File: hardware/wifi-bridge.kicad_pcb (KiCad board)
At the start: 4 copper layers, 50 x 35 mm, 78 parts, among them J201 USB-MINI-B-SMD, P101 CONN_1, P102 CONN_1, P103 CONN_1, P104 CON-SENSOR, Q101 MOS_P, SW101 ERASE, SW102 RESET, U101 AT91SAM3SXB, U102 ESP8266_WROOM02, U103 M24C64, U104 DRILL, U105 DRILL, U106 DRILL, U107 DRILL, U201 82400152, U202 AAT3681A, U203 PAM2301, U204 FAN4860, X101 16MHz

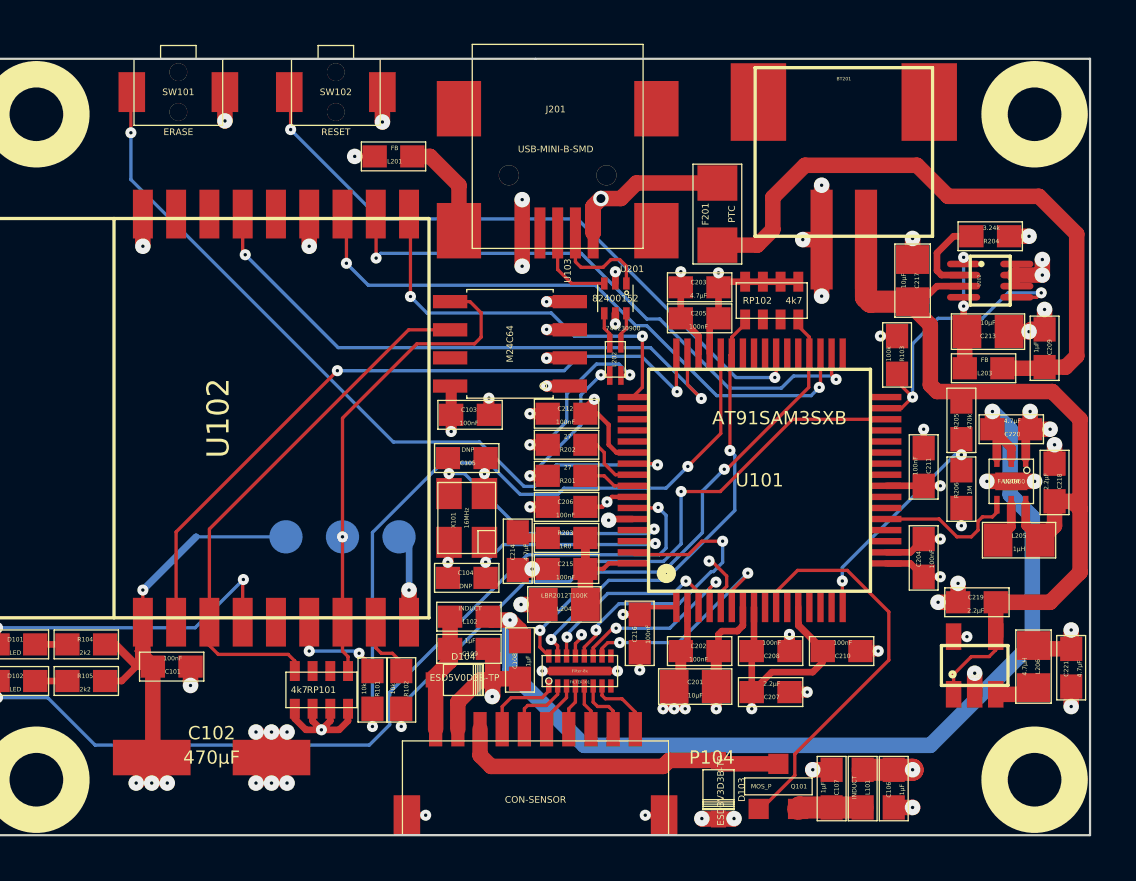
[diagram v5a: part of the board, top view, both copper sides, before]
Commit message: add planes, add logos etc.
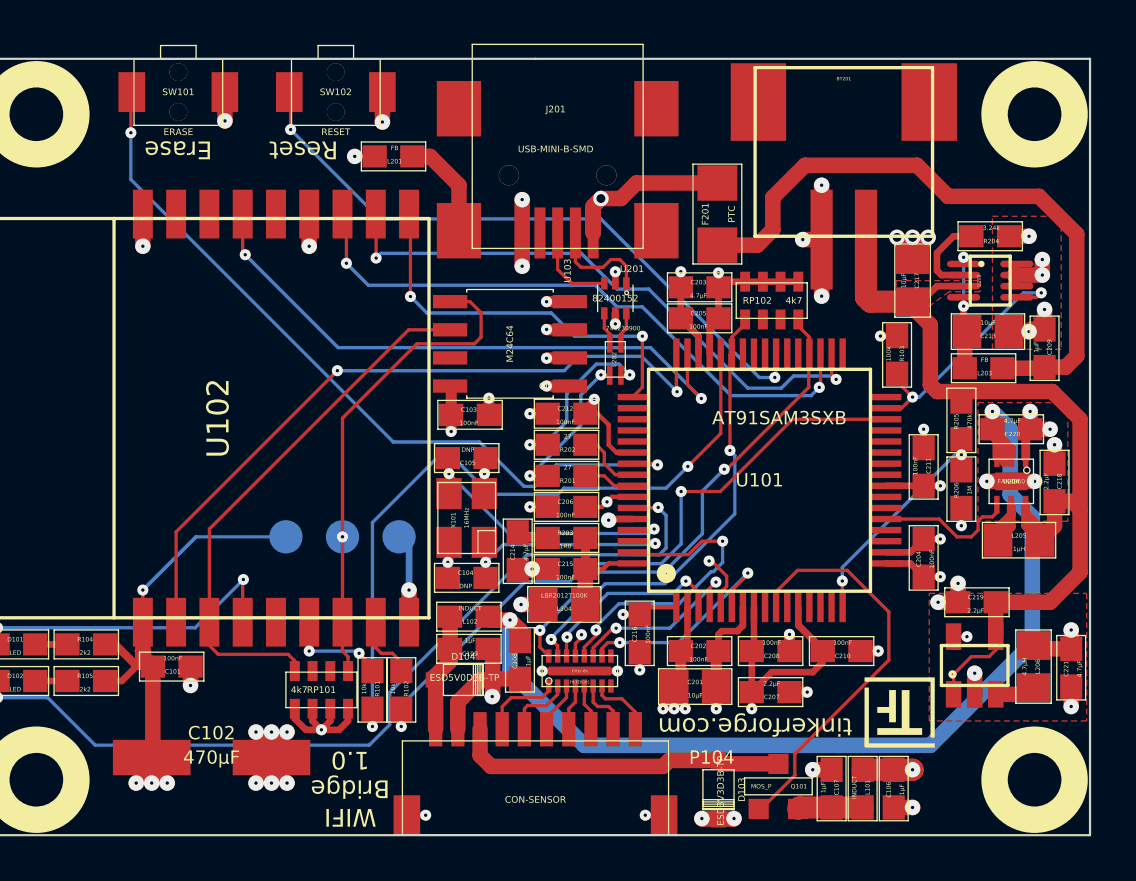
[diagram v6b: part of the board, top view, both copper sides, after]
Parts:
- added G***: Logo_31x31, kicad-libraries:Logo_31x31, F.Cu at (165.8, 46.2)
- added VAL: WEEE_7mm_back, kicad-libraries:WEEE_7mm_back, B.Cu at (147.8, 36.9)
- added VAL: CE_5mm, kicad-libraries:CE_5mm, B.Cu at (147.8, 26.8)
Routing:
- net Net-(C207-Pad1): track 58.6 -> 61.1 mm
- net GND: track 280.6 -> 282.9 mm, vias 64 -> 66
- net VCC: track 41.7 -> 43.5 mm
- net +5V: track 46.4 -> 48.1 mm
- net CHST: track 13.1 -> 11.7 mm
- net Net-(L205-Pad2): track 1.85 -> 3.25 mm
- added copper zone on VCC, net 3V3
- added copper zone on F.Cu, net GND
- added copper zone on GND, net GND
- added copper zone on F.Cu, net VCC
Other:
- board text added: "3V3"
- board text added: "DBG"
- board text added: "Erase"
- board text added: "GND"
- board text added: "Reset"
- board text added: "WIFI Bridge 1.0"
- board text added: "tinkerforge.com"

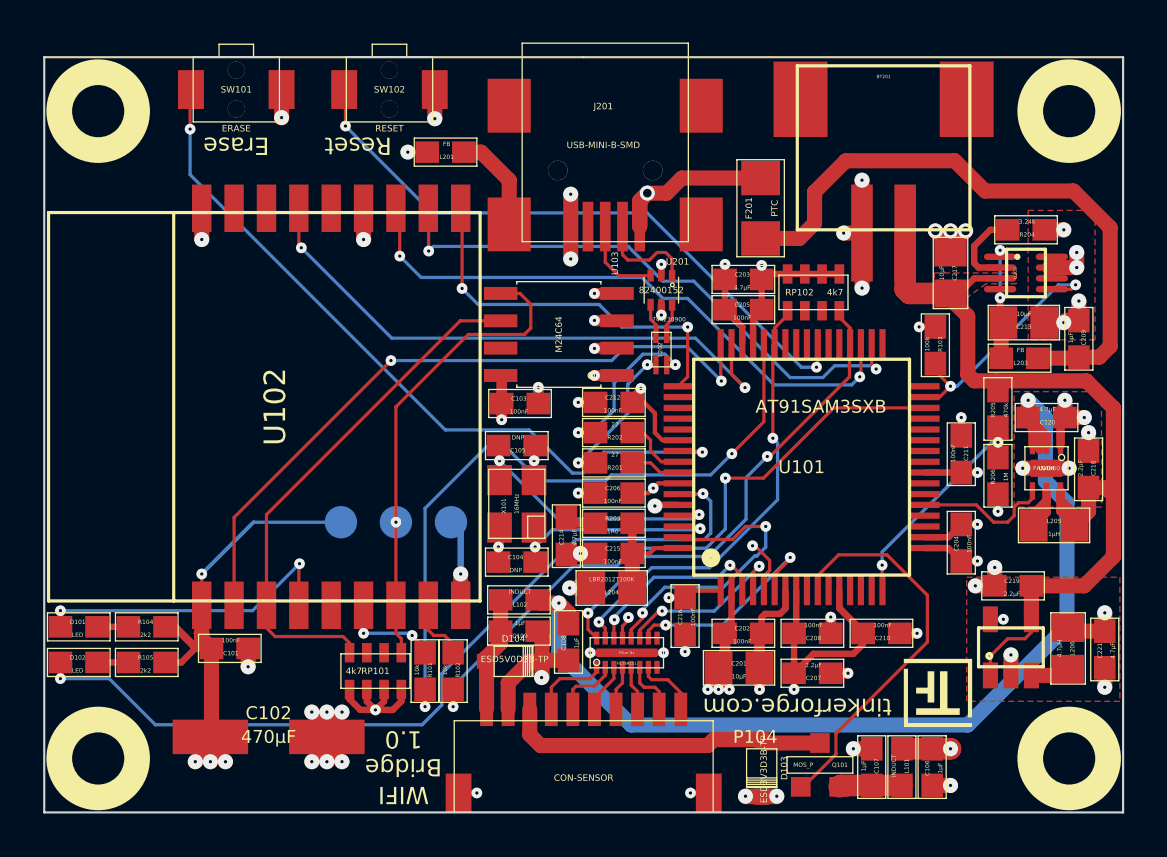
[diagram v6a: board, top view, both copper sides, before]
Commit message: round corners
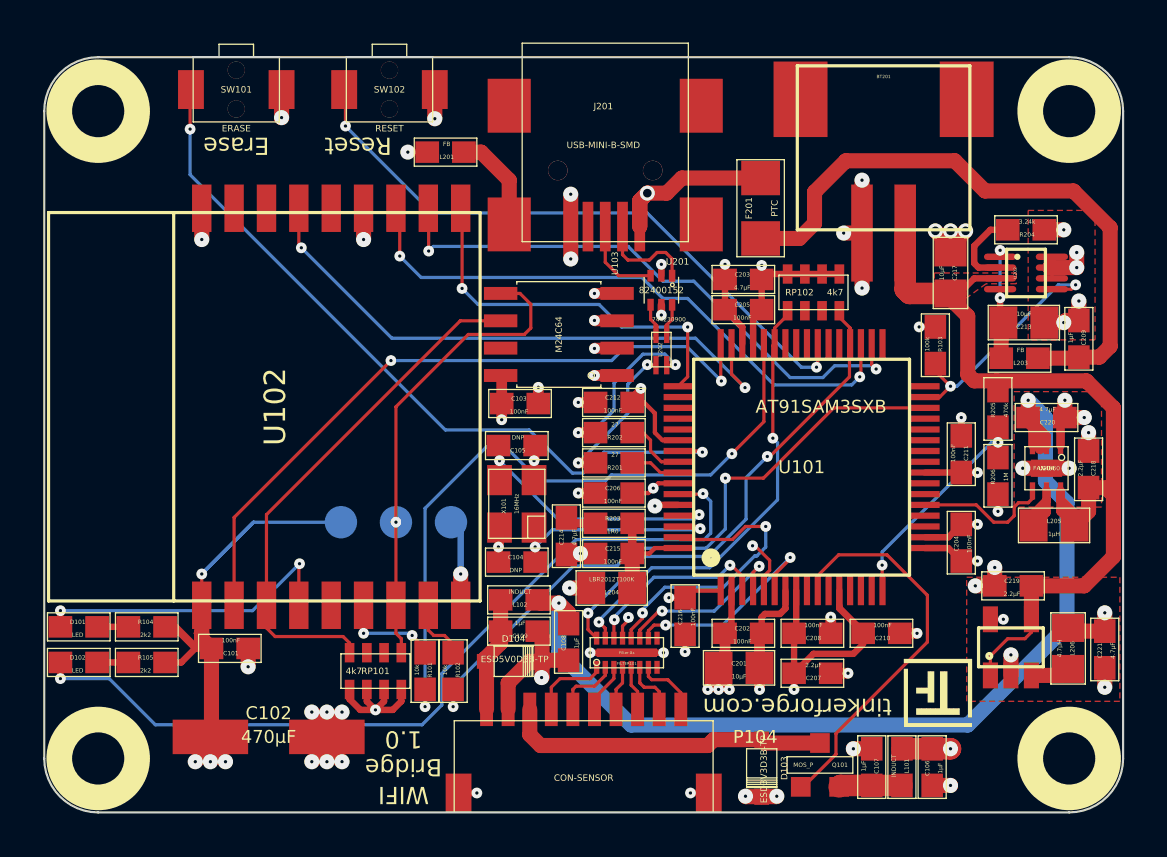
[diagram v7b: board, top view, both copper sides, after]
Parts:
- turned VAL to 0 degrees
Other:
- outline, holes or cut-outs redrawn
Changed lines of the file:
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@@
     (area 122.749999 15.149999 172.850001 50.250001)
     (thickness 1.6)
-    (drawings 12)
+    (drawings 15)
     (tracks 1047)
     (zones 0)
@@
     (aux_axis_origin 147.8 15.2)
     (grid_origin 147.8 15.2)
-    (visible_elements FFFFBF7F)
+    (visible_elements FFFFFF7F)
     (pcbplotparams
-      (layerselection 0x00030_80000001)
+      (layerselection 0x010f0_80000007)
       (usegerberextensions false)
       (excludeedgelayer true)
@@
       (outputformat 1)
       (mirror false)
-      (drillshape 1)
+      (drillshape 0)
       (scaleselection 1)
-      (outputdirectory /tmp/))
+      (outputdirectory /tmp/wifi/))
   )
   (net 0 "")
@@
   )
   (module kicad-libraries:CE_5mm (layer B.Cu)
-    (at 147.8 26.8 180)
-    (fp_text reference VAL (at 0 0 180) (layer B.SilkS) hide
+    (at 147.8 26.8)
+    (fp_text reference VAL (at 0 0) (layer B.SilkS) hide
       (effects (font (size 1.143 1.143) (thickness 0.1778)) (justify mirror))
     )
-    (fp_text value CE_5mm (at 0 0 180) (layer B.SilkS) hide
+    (fp_text value CE_5mm (at 0 0) (layer B.SilkS) hide
       (effects (font (size 1.143 1.143) (thickness 0.1778)) (justify mirror))
     )
@@
       (xy 2.3114 -1.41732) (xy 2.3114 -1.67132) (xy 2.3114 -1.67132)) (layer B.SilkS) (width 0.00254))
   )
+  (gr_line (start 172.8 47.7) (end 172.8 17.7) (angle 90) (layer Edge.Cuts) (width 0.1))
+  (gr_line (start 170.3 50.2) (end 125.3 50.2) (angle 90) (layer Edge.Cuts) (width 0.1))
+  (gr_line (start 122.8 17.7) (end 122.8 47.7) (angle 90) (layer Edge.Cuts) (width 0.1))
+  (gr_line (start 170.3 15.2) (end 125.3 15.2) (angle 90) (layer Edge.Cuts) (width 0.1))
+  (gr_arc (start 125.3 17.7) (end 122.8 17.7) (angle 90) (layer Edge.Cuts) (width 0.1))
+  (gr_arc (start 125.3 47.7) (end 125.3 50.2) (angle 90) (layer Edge.Cuts) (width 0.1))
+  (gr_arc (start 170.3 47.7) (end 172.8 47.7) (angle 90) (layer Edge.Cuts) (width 0.1))
+  (gr_arc (start 170.3 17.7) (end 170.3 15.2) (angle 90) (layer Edge.Cuts) (width 0.1))
   (gr_text GND (at 141.65 34.6 90) (layer B.SilkS)
     (effects (font (size 0.8 0.8) (thickness 0.15)) (justify mirror))
@@
     (effects (font (size 0.8 0.8) (thickness 0.15)) (justify mirror))
   )
-  (gr_text 3V3 (at 136.55 34.6 270) (layer B.SilkS)
+  (gr_text 3V3 (at 136.55 34.6 90) (layer B.SilkS)
     (effects (font (size 0.8 0.8) (thickness 0.15)) (justify mirror))
   )
@@
     (effects (font (size 0.8 0.8) (thickness 0.15)))
   )
-  (gr_line (start 172.8 15.2) (end 172.8 50.2) (angle 90) (layer Edge.Cuts) (width 0.1))
-  (gr_line (start 122.8 50.2) (end 122.8 15.2) (angle 90) (layer Edge.Cuts) (width 0.1))
-  (gr_line (start 172.8 15.2) (end 147.8 15.2) (angle 90) (layer Edge.Cuts) (width 0.1))
-  (gr_line (start 122.8 50.2) (end 172.8 50.2) (angle 90) (layer Edge.Cuts) (width 0.1))
-  (gr_line (start 147.8 15.2) (end 122.8 15.2) (angle 90) (layer Edge.Cuts) (width 0.1))
   (segment (start 164.8 24.25) (end 164.8 23.95) (width 0.7) (layer F.Cu) (net 1))
   (segment (start 164.8 23.95) (end 164.1 23.25) (width 0.7) (layer F.Cu) (net 1))

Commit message: version for prototype order
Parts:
- added Fiducial_Mark: VAL**, kicad-libraries:Fiducial_Mark, F.Cu at (127.8, 20.7)
- added Fiducial_Mark: VAL**, kicad-libraries:Fiducial_Mark, F.Cu at (162.8, 16.7)
- added Fiducial_Mark: VAL**, kicad-libraries:Fiducial_Mark, F.Cu at (166.3, 48.7)
